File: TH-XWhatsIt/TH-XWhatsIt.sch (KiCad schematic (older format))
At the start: 27 parts, among them J1 COLUMNS, J12 EXPANSION HEADER, J2 ROWS, U1 LM339, U2 MCP4921-EP, U3 74HCT595, U5 74HCT595, U6 LM339, U7 ProMicro, U8 74HCT595

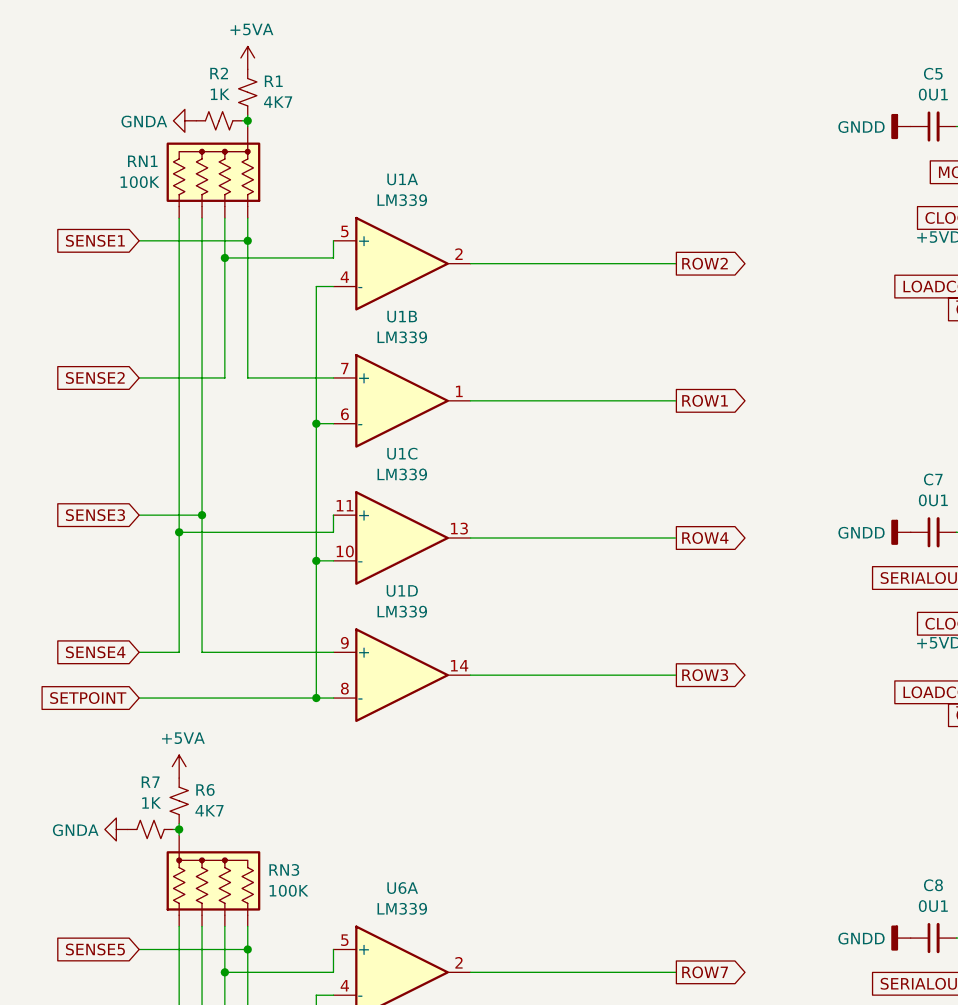
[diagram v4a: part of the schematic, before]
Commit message: Remove extra biasing resistors. Better for >4row keyboards.
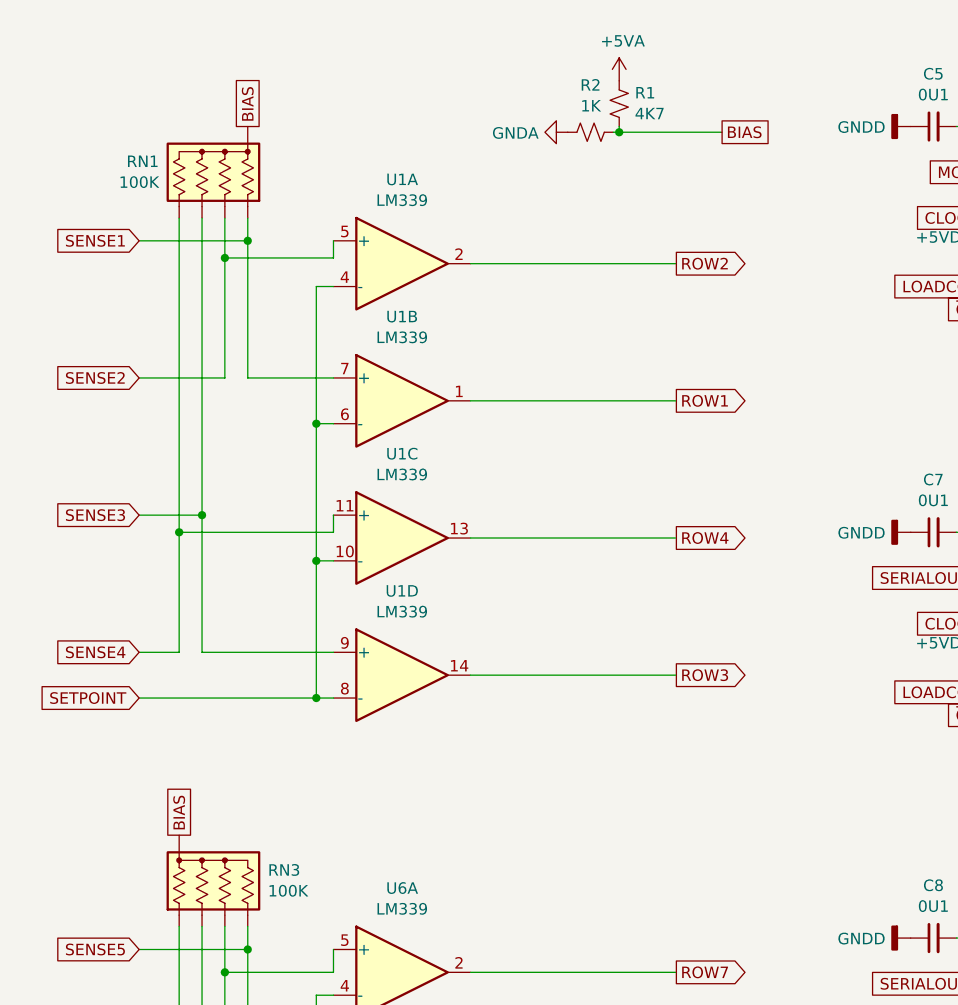
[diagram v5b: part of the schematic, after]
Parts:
- removed R6: 4K7, Resistor_THT:R_Axial_DIN0204_L3.6mm_D1.6mm_P1.90mm_Vertical, symbol Device:R_Small_US
- removed R7: 1K, Resistor_THT:R_Axial_DIN0204_L3.6mm_D1.6mm_P1.90mm_Vertical, symbol Device:R_Small_US
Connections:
- net BIAS: now reaches RN3.1 (common)
- net BIAS: now also R1.2, R2.1, RN1.1 (common)
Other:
- moved on the sheet: R1, R2
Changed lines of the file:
@@
-$EndComp
-$Comp
-L Device:R_Small_US R6
-U 1 1 5E3286E3
-P 1325 3925
-F 0 "R6" H 1393 3971 50  0000 L CNN
-F 1 "4K7" H 1393 3880 50  0000 L CNN
-F 2 "Resistor_THT:R_Axial_DIN0204_L3.6mm_D1.6mm_P1.90mm_Vertical" H 1325 3925 50  0001 C CNN
-F 3 "~" H 1325 3925 50  0001 C CNN
-	1    1325 3925
-	1    0    0    -1
 $EndComp
 $Comp
@@
 	1    0    0    -1
 $EndComp
-$Comp
-L Device:R_Small_US R7
-U 1 1 5E34214B
-P 1200 4050
-F 0 "R7" V 995 4050 50  0000 C CNN
-F 1 "1K" V 1086 4050 50  0000 C CNN
-F 2 "Resistor_THT:R_Axial_DIN0204_L3.6mm_D1.6mm_P1.90mm_Vertical" H 1200 4050 50  0001 C CNN
-F 3 "~" H 1200 4050 50  0001 C CNN
-	1    1200 4050
-	0    1    1    0
-$EndComp
-Wire Wire Line
-	1325 4025 1325 4050
-Wire Wire Line
-	1300 4050 1325 4050
-Connection ~ 1325 4050
-Wire Wire Line
-	1325 4050 1325 4075
 Wire Wire Line
 	2000 4775 1925 4775
@@
 	1    0    0    -1
 $EndComp
-$Comp
-L Device:R_Small_US R1
-U 1 1 5E3E384B
-P 1625 825
-F 0 "R1" H 1693 871 50  0000 L CNN
-F 1 "4K7" H 1693 780 50  0000 L CNN
-F 2 "Resistor_THT:R_Axial_DIN0204_L3.6mm_D1.6mm_P1.90mm_Vertical" H 1625 825 50  0001 C CNN
-F 3 "~" H 1625 825 50  0001 C CNN
-	1    1625 825
-	1    0    0    -1
-$EndComp
-$Comp
-L Device:R_Network04_US RN1
-U 1 1 5E3E3857
-P 1425 1175
-F 0 "RN1" H 1613 1221 50  0000 L CNN
-F 1 "100K" H 1613 1130 50  0000 L CNN
-F 2 "Resistor_THT:R_Array_SIP5" V 1700 1175 50  0001 C CNN
-F 3 "http://www.vishay.com/docs/31509/csc.pdf" H 1425 1175 50  0001 C CNN
-	1    1425 1175
-	-1   0    0    -1
-$EndComp
-$Comp
-L Device:R_Small_US R2
-U 1 1 5E3E385D
-P 1500 950
-F 0 "R2" V 1295 950 50  0000 C CNN
-F 1 "1K" V 1386 950 50  0000 C CNN
-F 2 "Resistor_THT:R_Axial_DIN0204_L3.6mm_D1.6mm_P1.90mm_Vertical" H 1500 950 50  0001 C CNN
-F 3 "~" H 1500 950 50  0001 C CNN
-	1    1500 950
-	0    1    1    0
-$EndComp
-Wire Wire Line
-	1625 925  1625 950
-Wire Wire Line
-	1600 950  1625 950
-Connection ~ 1625 950
-Wire Wire Line
-	1625 950  1625 975
+Wire Wire Line
+	3250 975  3250 1000
+Wire Wire Line
+	3225 1000 3250 1000
 Wire Wire Line
 	2000 1675 1925 1675
@@
 $EndComp
 $Comp
-L power:+5VA #PWR0103
-U 1 1 5E8155F5
-P 1625 725
-F 0 "#PWR0103" H 1625 575 50  0001 C CNN
-F 1 "+5VA" H 1640 898 50  0000 C CNN
-F 2 "" H 1625 725 50  0001 C CNN
-F 3 "" H 1625 725 50  0001 C CNN
-	1    1625 725
-	1    0    0    -1
-$EndComp
-$Comp
 L power:+5VD #PWR0106
 U 1 1 5E817D6B
@@
 F 3 "" H 8575 875 50  0001 C CNN
 	1    8575 875
-	1    0    0    -1
-$EndComp
-$Comp
-L power:+5VA #PWR0112
-U 1 1 5E81CA85
-P 1325 3825
-F 0 "#PWR0112" H 1325 3675 50  0001 C CNN
-F 1 "+5VA" H 1340 3998 50  0000 C CNN
-F 2 "" H 1325 3825 50  0001 C CNN
-F 3 "" H 1325 3825 50  0001 C CNN
-	1    1325 3825
 	1    0    0    -1
 $EndComp
@@
 F 3 "" H 1250 6950 50  0001 C CNN
 	1    1250 6950
-	0    1    1    0
-$EndComp
-$Comp
-L power:GNDA #PWR0140
-U 1 1 5E847CED
-P 1400 950
-F 0 "#PWR0140" H 1400 700 50  0001 C CNN
-F 1 "GNDA" V 1405 823 50  0000 R CNN
-F 2 "" H 1400 950 50  0001 C CNN
-F 3 "" H 1400 950 50  0001 C CNN
-	1    1400 950
-	0    1    1    0
-$EndComp
-$Comp
-L power:GNDA #PWR0141
-U 1 1 5E847FAD
-P 1100 4050
-F 0 "#PWR0141" H 1100 3800 50  0001 C CNN
-F 1 "GNDA" V 1105 3923 50  0000 R CNN
-F 2 "" H 1100 4050 50  0001 C CNN
-F 3 "" H 1100 4050 50  0001 C CNN
-	1    1100 4050
 	0    1    1    0
 $EndComp
@@
 Wire Wire Line
 	2600 6475 3500 6475
+$Comp
+L Device:R_Small_US R2
+U 1 1 5E3E385D
+P 3125 1000
+F 0 "R2" V 2920 1000 50  0000 C CNN
+F 1 "1K" V 3011 1000 50  0000 C CNN
+F 2 "Resistor_THT:R_Axial_DIN0204_L3.6mm_D1.6mm_P1.90mm_Vertical" H 3125 1000 50  0001 C CNN
+F 3 "~" H 3125 1000 50  0001 C CNN
+	1    3125 1000
+	0    1    1    0
+$EndComp
+$Comp
+L power:GNDA #PWR0140
+U 1 1 5E847CED
+P 3025 1000
+F 0 "#PWR0140" H 3025 750 50  0001 C CNN
+F 1 "GNDA" V 3030 873 50  0000 R CNN
+F 2 "" H 3025 1000 50  0001 C CNN
+F 3 "" H 3025 1000 50  0001 C CNN
+	1    3025 1000
+	0    1    1    0
+$EndComp
+$Comp
+L power:+5VA #PWR0103
+U 1 1 5E8155F5
+P 3250 775
+F 0 "#PWR0103" H 3250 625 50  0001 C CNN
+F 1 "+5VA" H 3265 948 50  0000 C CNN
+F 2 "" H 3250 775 50  0001 C CNN
+F 3 "" H 3250 775 50  0001 C CNN
+	1    3250 775
+	1    0    0    -1
+$EndComp
+$Comp
+L Device:R_Small_US R1
+U 1 1 5E3E384B
+P 3250 875
+F 0 "R1" H 3318 921 50  0000 L CNN
+F 1 "4K7" H 3318 830 50  0000 L CNN
+F 2 "Resistor_THT:R_Axial_DIN0204_L3.6mm_D1.6mm_P1.90mm_Vertical" H 3250 875 50  0001 C CNN
+F 3 "~" H 3250 875 50  0001 C CNN
+	1    3250 875
+	1    0    0    -1
+$EndComp
+Text GLabel 3700 1000 2    50   UnSpc ~ 0
+BIAS
+Wire Wire Line
+	3250 1000 3700 1000
+Connection ~ 3250 1000
+Text GLabel 1625 975  1    50   UnSpc ~ 0
+BIAS
+$Comp
+L Device:R_Network04_US RN1
+U 1 1 5E3E3857
+P 1425 1175
+F 0 "RN1" H 1613 1221 50  0000 L CNN
+F 1 "100K" H 1613 1130 50  0000 L CNN
+F 2 "Resistor_THT:R_Array_SIP5" V 1700 1175 50  0001 C CNN
+F 3 "http://www.vishay.com/docs/31509/csc.pdf" H 1425 1175 50  0001 C CNN
+	1    1425 1175
+	-1   0    0    -1
+$EndComp
+Text GLabel 1325 4075 1    50   UnSpc ~ 0
+BIAS
 $EndSCHEMATC

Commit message: Made DAC output resistors horizontal
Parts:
- R3, R4, R5: footprint Resistor_THT:R_Axial_DIN0204_L3.6mm_D1.6mm_P1.90mm_Vertical -> Resistor_THT:R_Axial_DIN0204_L3.6mm_D1.6mm_P7.62mm_Horizontal
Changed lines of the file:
@@
 F 0 "R4" V 9945 1400 50  0000 C CNN
 F 1 "20K" V 10036 1400 50  0000 C CNN
-F 2 "Resistor_THT:R_Axial_DIN0204_L3.6mm_D1.6mm_P1.90mm_Vertical" H 10150 1400 50  0001 C CNN
+F 2 "Resistor_THT:R_Axial_DIN0204_L3.6mm_D1.6mm_P7.62mm_Horizontal" H 10150 1400 50  0001 C CNN
 F 3 "~" H 10150 1400 50  0001 C CNN
 	1    10150 1400
@@
 F 0 "R3" H 10207 1229 50  0000 R CNN
 F 1 "20K" H 10207 1320 50  0000 R CNN
-F 2 "Resistor_THT:R_Axial_DIN0204_L3.6mm_D1.6mm_P1.90mm_Vertical" H 10275 1275 50  0001 C CNN
+F 2 "Resistor_THT:R_Axial_DIN0204_L3.6mm_D1.6mm_P7.62mm_Horizontal" H 10275 1275 50  0001 C CNN
 F 3 "~" H 10275 1275 50  0001 C CNN
 	1    10275 1275
@@
 F 0 "R5" H 10207 1479 50  0000 R CNN
 F 1 "4K7" H 10207 1570 50  0000 R CNN
-F 2 "Resistor_THT:R_Axial_DIN0204_L3.6mm_D1.6mm_P1.90mm_Vertical" H 10275 1525 50  0001 C CNN
+F 2 "Resistor_THT:R_Axial_DIN0204_L3.6mm_D1.6mm_P7.62mm_Horizontal" H 10275 1525 50  0001 C CNN
 F 3 "~" H 10275 1525 50  0001 C CNN
 	1    10275 1525

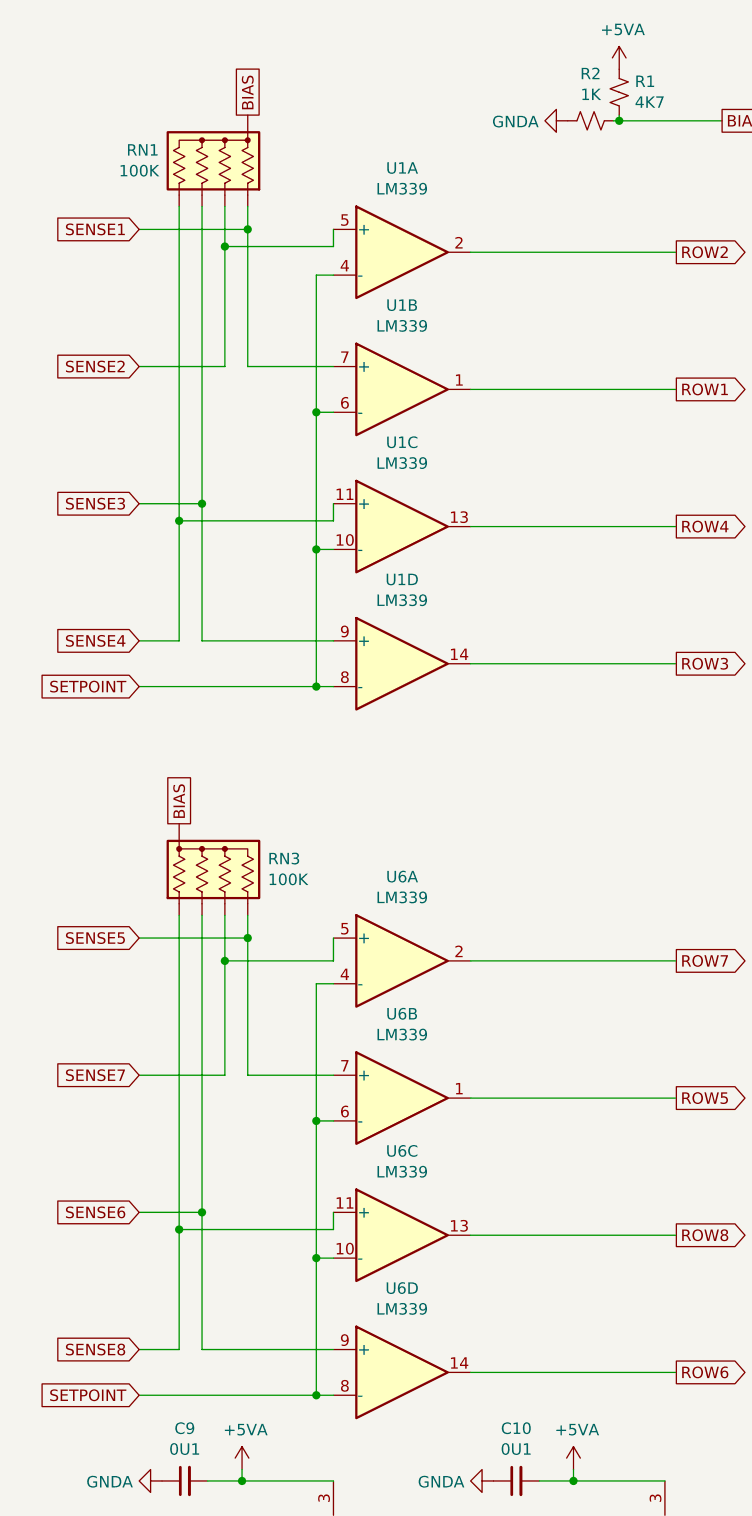
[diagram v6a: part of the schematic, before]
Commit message: Add option to use individual resistors to pull towards bias
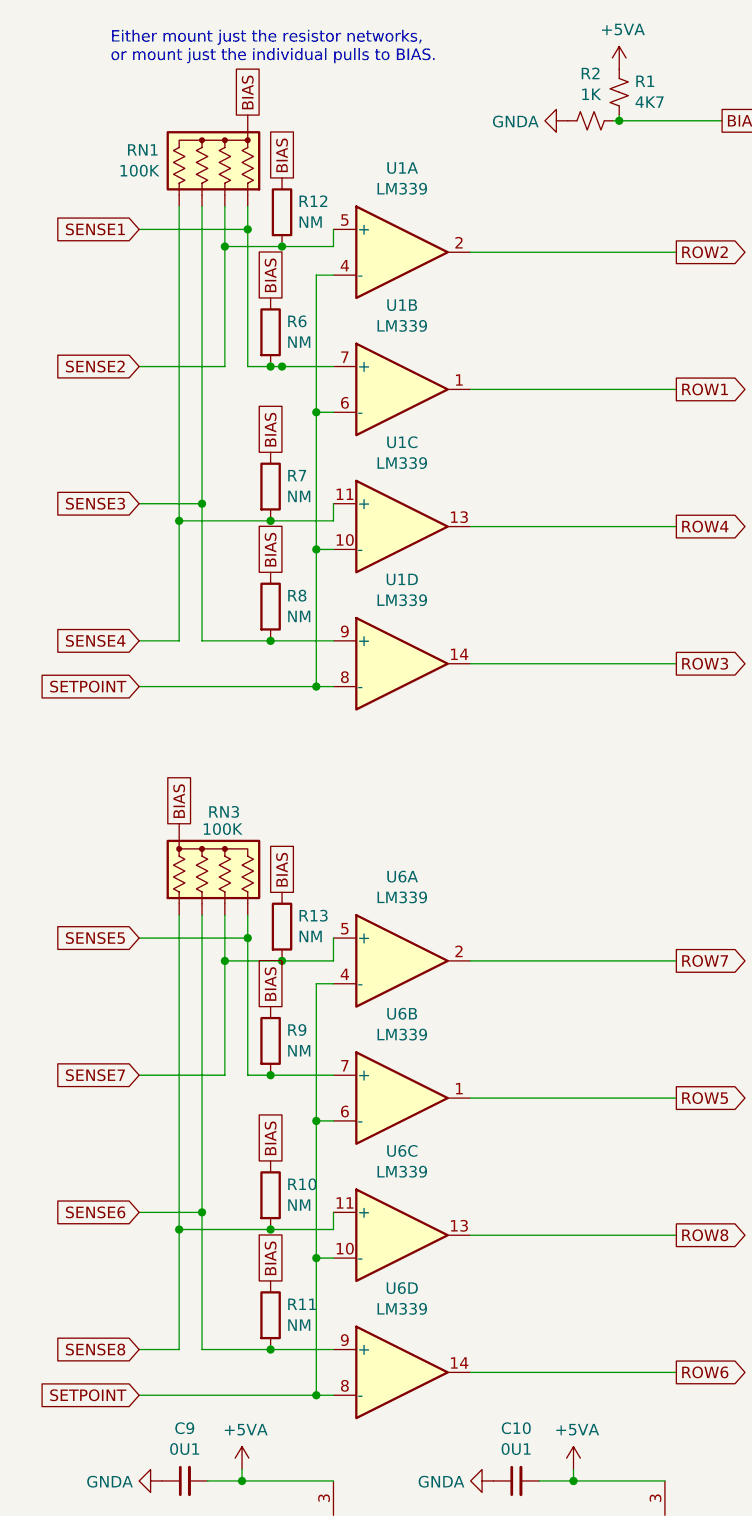
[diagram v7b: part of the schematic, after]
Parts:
- added R10, R11, R12, R13, R6, R7, R8, R9: NM, Resistor_THT:R_Axial_DIN0204_L3.6mm_D1.6mm_P7.62mm_Horizontal, symbol Device:R
- R1, R2: footprint Resistor_THT:R_Axial_DIN0204_L3.6mm_D1.6mm_P1.90mm_Vertical -> Resistor_THT:R_Axial_DIN0204_L3.6mm_D1.6mm_P7.62mm_Horizontal
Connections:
- net BIAS: now also R10.1, R11.1, R12.1, R13.1, R6.1, R7.1, R8.1, R9.1
- net SENSE1: now also R6.2
- net SENSE2: now also R12.2
- net SENSE3: now also R8.2
- net SENSE4: now also R7.2
- net SENSE5: now also R9.2
- net SENSE6: now also R11.2
- net SENSE7: now also R13.2
- net SENSE8: now also R10.2
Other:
- note added: "Either mount just the resistor networks,\nor mount just the individual pulls to BIAS."
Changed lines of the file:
@@
 U 1 1 5E33600B
 P 1525 4275
-F 0 "RN3" H 1713 4321 50  0000 L CNN
-F 1 "100K" H 1713 4230 50  0000 L CNN
+F 0 "RN3" H 1450 4525 50  0000 L CNN
+F 1 "100K" H 1425 4450 50  0000 L CNN
 F 2 "Resistor_THT:R_Array_SIP5" V 1800 4275 50  0001 C CNN
 F 3 "http://www.vishay.com/docs/31509/csc.pdf" H 1525 4275 50  0001 C CNN
@@
 	1625 4575 1625 5175
 Wire Wire Line
-	1625 5175 2000 5175
+	1625 5175 1725 5175
 Connection ~ 1625 4575
 Wire Wire Line
-	1525 4675 2000 4675
+	1525 4675 1775 4675
 Wire Wire Line
 	2000 4675 2000 4575
@@
 	1525 4675 1525 4475
 Wire Wire Line
-	1325 5850 2000 5850
+	1325 5850 1725 5850
 Wire Wire Line
 	2000 5850 2000 5775
@@
 	1425 5775 1425 6375
 Wire Wire Line
-	1425 6375 2000 6375
+	1425 6375 1725 6375
 Connection ~ 1425 5775
 Text GLabel 3500 5875 2    50   Output ~ 0
@@
 ROW7
 Wire Wire Line
-	2000 2075 1625 2075
+	2000 2075 1775 2075
 Wire Wire Line
 	1625 2075 1625 1475
 Connection ~ 1625 1475
 Wire Wire Line
-	1525 1550 2000 1550
+	1525 1550 1775 1550
 Wire Wire Line
 	2000 1550 2000 1475
@@
 	1525 1550 1525 1375
 Wire Wire Line
-	2000 3275 1425 3275
+	2000 3275 1725 3275
 Wire Wire Line
 	1425 3275 1425 2675
 Connection ~ 1425 2675
 Wire Wire Line
-	1325 2750 2000 2750
+	1325 2750 1725 2750
 Wire Wire Line
 	2000 2750 2000 2675
@@
 F 0 "R2" V 2920 1000 50  0000 C CNN
 F 1 "1K" V 3011 1000 50  0000 C CNN
-F 2 "Resistor_THT:R_Axial_DIN0204_L3.6mm_D1.6mm_P1.90mm_Vertical" H 3125 1000 50  0001 C CNN
+F 2 "Resistor_THT:R_Axial_DIN0204_L3.6mm_D1.6mm_P7.62mm_Horizontal" H 3125 1000 50  0001 C CNN
 F 3 "~" H 3125 1000 50  0001 C CNN
 	1    3125 1000
@@
 F 0 "R1" H 3318 921 50  0000 L CNN
 F 1 "4K7" H 3318 830 50  0000 L CNN
-F 2 "Resistor_THT:R_Axial_DIN0204_L3.6mm_D1.6mm_P1.90mm_Vertical" H 3250 875 50  0001 C CNN
+F 2 "Resistor_THT:R_Axial_DIN0204_L3.6mm_D1.6mm_P7.62mm_Horizontal" H 3250 875 50  0001 C CNN
 F 3 "~" H 3250 875 50  0001 C CNN
 	1    3250 875
@@
 Text GLabel 1325 4075 1    50   UnSpc ~ 0
 BIAS
+$Comp
+L Device:R R12
+U 1 1 5F41CB12
+P 1775 1400
+F 0 "R12" H 1845 1446 50  0000 L CNN
+F 1 "NM" H 1845 1355 50  0000 L CNN
+F 2 "Resistor_THT:R_Axial_DIN0204_L3.6mm_D1.6mm_P7.62mm_Horizontal" V 1705 1400 50  0001 C CNN
+F 3 "~" H 1775 1400 50  0001 C CNN
+	1    1775 1400
+	1    0    0    -1
+$EndComp
+Connection ~ 1775 1550
+Wire Wire Line
+	1775 1550 2000 1550
+$Comp
+L Device:R R6
+U 1 1 5F420594
+P 1725 1925
+F 0 "R6" H 1795 1971 50  0000 L CNN
+F 1 "NM" H 1795 1880 50  0000 L CNN
+F 2 "Resistor_THT:R_Axial_DIN0204_L3.6mm_D1.6mm_P7.62mm_Horizontal" V 1655 1925 50  0001 C CNN
+F 3 "~" H 1725 1925 50  0001 C CNN
+	1    1725 1925
+	1    0    0    -1
+$EndComp
+Connection ~ 1775 2075
+Wire Wire Line
+	1775 2075 1725 2075
+Connection ~ 1725 2075
+Wire Wire Line
+	1725 2075 1625 2075
+$Comp
+L Device:R R7
+U 1 1 5F42305A
+P 1725 2600
+F 0 "R7" H 1795 2646 50  0000 L CNN
+F 1 "NM" H 1795 2555 50  0000 L CNN
+F 2 "Resistor_THT:R_Axial_DIN0204_L3.6mm_D1.6mm_P7.62mm_Horizontal" V 1655 2600 50  0001 C CNN
+F 3 "~" H 1725 2600 50  0001 C CNN
+	1    1725 2600
+	1    0    0    -1
+$EndComp
+Connection ~ 1725 2750
+Wire Wire Line
+	1725 2750 2000 2750
+$Comp
+L Device:R R8
+U 1 1 5F42370C
+P 1725 3125
+F 0 "R8" H 1795 3171 50  0000 L CNN
+F 1 "NM" H 1795 3080 50  0000 L CNN
+F 2 "Resistor_THT:R_Axial_DIN0204_L3.6mm_D1.6mm_P7.62mm_Horizontal" V 1655 3125 50  0001 C CNN
+F 3 "~" H 1725 3125 50  0001 C CNN
+	1    1725 3125
+	1    0    0    -1
+$EndComp
+Connection ~ 1725 3275
+Wire Wire Line
+	1725 3275 1425 3275
+$Comp
+L Device:R R13
+U 1 1 5F426116
+P 1775 4525
+F 0 "R13" H 1845 4571 50  0000 L CNN
+F 1 "NM" H 1845 4480 50  0000 L CNN
+F 2 "Resistor_THT:R_Axial_DIN0204_L3.6mm_D1.6mm_P7.62mm_Horizontal" V 1705 4525 50  0001 C CNN
+F 3 "~" H 1775 4525 50  0001 C CNN
+	1    1775 4525
+	1    0    0    -1
+$EndComp
+Connection ~ 1775 4675
+Wire Wire Line
+	1775 4675 2000 4675
+$Comp
+L Device:R R9
+U 1 1 5F4267D3
+P 1725 5025
+F 0 "R9" H 1795 5071 50  0000 L CNN
+F 1 "NM" H 1795 4980 50  0000 L CNN
+F 2 "Resistor_THT:R_Axial_DIN0204_L3.6mm_D1.6mm_P7.62mm_Horizontal" V 1655 5025 50  0001 C CNN
+F 3 "~" H 1725 5025 50  0001 C CNN
+	1    1725 5025
+	1    0    0    -1
+$EndComp
+Connection ~ 1725 5175
+Wire Wire Line
+	1725 5175 2000 5175
+$Comp
+L Device:R R10
+U 1 1 5F4281A3
+P 1725 5700
+F 0 "R10" H 1795 5746 50  0000 L CNN
+F 1 "NM" H 1795 5655 50  0000 L CNN
+F 2 "Resistor_THT:R_Axial_DIN0204_L3.6mm_D1.6mm_P7.62mm_Horizontal" V 1655 5700 50  0001 C CNN
+F 3 "~" H 1725 5700 50  0001 C CNN
+	1    1725 5700
+	1    0    0    -1
+$EndComp
+Connection ~ 1725 5850
+Wire Wire Line
+	1725 5850 2000 5850
+$Comp
+L Device:R R11
+U 1 1 5F428763
+P 1725 6225
+F 0 "R11" H 1795 6271 50  0000 L CNN
+F 1 "NM" H 1795 6180 50  0000 L CNN
+F 2 "Resistor_THT:R_Axial_DIN0204_L3.6mm_D1.6mm_P7.62mm_Horizontal" V 1655 6225 50  0001 C CNN
+F 3 "~" H 1725 6225 50  0001 C CNN
+	1    1725 6225
+	1    0    0    -1
+$EndComp
+Connection ~ 1725 6375
+Wire Wire Line
+	1725 6375 2000 6375
+Text GLabel 1775 1250 1    50   UnSpc ~ 0
+BIAS
+Text GLabel 1725 1775 1    50   UnSpc ~ 0
+BIAS
+Text GLabel 1725 2450 1    50   UnSpc ~ 0
+BIAS
+Text GLabel 1725 2975 1    50   UnSpc ~ 0
+BIAS
+Text GLabel 1775 4375 1    50   UnSpc ~ 0
+BIAS
+Text GLabel 1725 4875 1    50   UnSpc ~ 0
+BIAS
+Text GLabel 1725 5550 1    50   UnSpc ~ 0
+BIAS
+Text GLabel 1725 6075 1    50   UnSpc ~ 0
+BIAS
+Text Notes 1025 750  0    50   ~ 0
+Either mount just the resistor networks,\nor mount just the individual pulls to BIAS.
 $EndSCHEMATC
